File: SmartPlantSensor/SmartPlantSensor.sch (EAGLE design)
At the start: 13 parts

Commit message: Release v1.0.0
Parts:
- removed C5: 10nF, rcl:C-EUC0603
- removed U$1: TLC555CDR, HeRo:TLC555CDR
- removed U$2: ESP-12E, HeRo:ESP-12E
- added C1: 10nF, rcl:C-EUC0603
- added DS18B20: DS18B20Z+, MaximIntegrated:DS18B20Z+
- added ESP-12E: ESP-12E, ESP:ESP-12E
- added JP10, JP11, JP12, JP13, JP14, JP3, JP4, JP5, JP6, JP7, JP8, JP9: (no value), pinhead:PINHD-1X1
- added R10, R11, R7, R8, R9: 10k, rcl:R-EU_R0603
- added TLC555: TLC555CD, TexasInstruments:TLC555CD
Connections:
- removed net N$7: C5.2, U$1.CONT
- new net 1WIRE: DS18B20.DQ, ESP-12E.IO4
- new net EN: ESP-12E.EN, R7.1
- new net IO0: ESP-12E.IO0, JP6.1, R9.1
- new net IO12: ESP-12E.IO12, JP12.1
- new net IO13: ESP-12E.IO13, JP11.1
- new net IO14: ESP-12E.IO14, JP13.1
- new net IO15: ESP-12E.IO15, R8.2
- new net IO16: ESP-12E.IO16, JP14.1
- new net IO2: ESP-12E.IO2, R11.1
- new net N$1: C1.2, TLC555.CONT
- new net RST: ESP-12E.RST, JP5.1, R10.1
- new net RXD: ESP-12E.RXD, JP8.1
- new net TXD: ESP-12E.TXD, JP7.1
- net +3V3: now also DS18B20.VDD, ESP-12E.VCC, JP3.1, JP9.1, R10.2, R11.2, R7.2, R9.2, TLC555.RST, TLC555.VDD; no longer U$1.RESET, U$1.VDD, U$2.VCC
- net ADC: now also ESP-12E.ADC; no longer U$2.ADC
- net DISH: now also TLC555.DISCH; no longer U$1.DISCH
- net GND: now also C1.1, DS18B20.GND, ESP-12E.GND, JP10.1, JP4.1, R8.1, TLC555.GND; no longer C5.1, U$1.GND, U$2.GND
- net OUT: now also TLC555.OUT; no longer U$1.OUT
- net T: now also TLC555.THRES, TLC555.TRIG; no longer U$1.THRES, U$1.TRIG
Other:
- note added: "Capacitive Moisture Sensor"
- note added: "ESP8266"
- note added: "ESP8266 I/O"
- note added: "ESP8266 PU/PD"
- note added: "Smart Plant Sensor"
- note added: "Temperature-Sensor"
- note added: "Voltage divider: 3.3V -> 1V"
- note added: "https://github.com/xXAM22Xx/SmartPlantSensor"
- note added: "v1.0.0"
- moved on the sheet: C3, C4, R1, R4, R5, R6

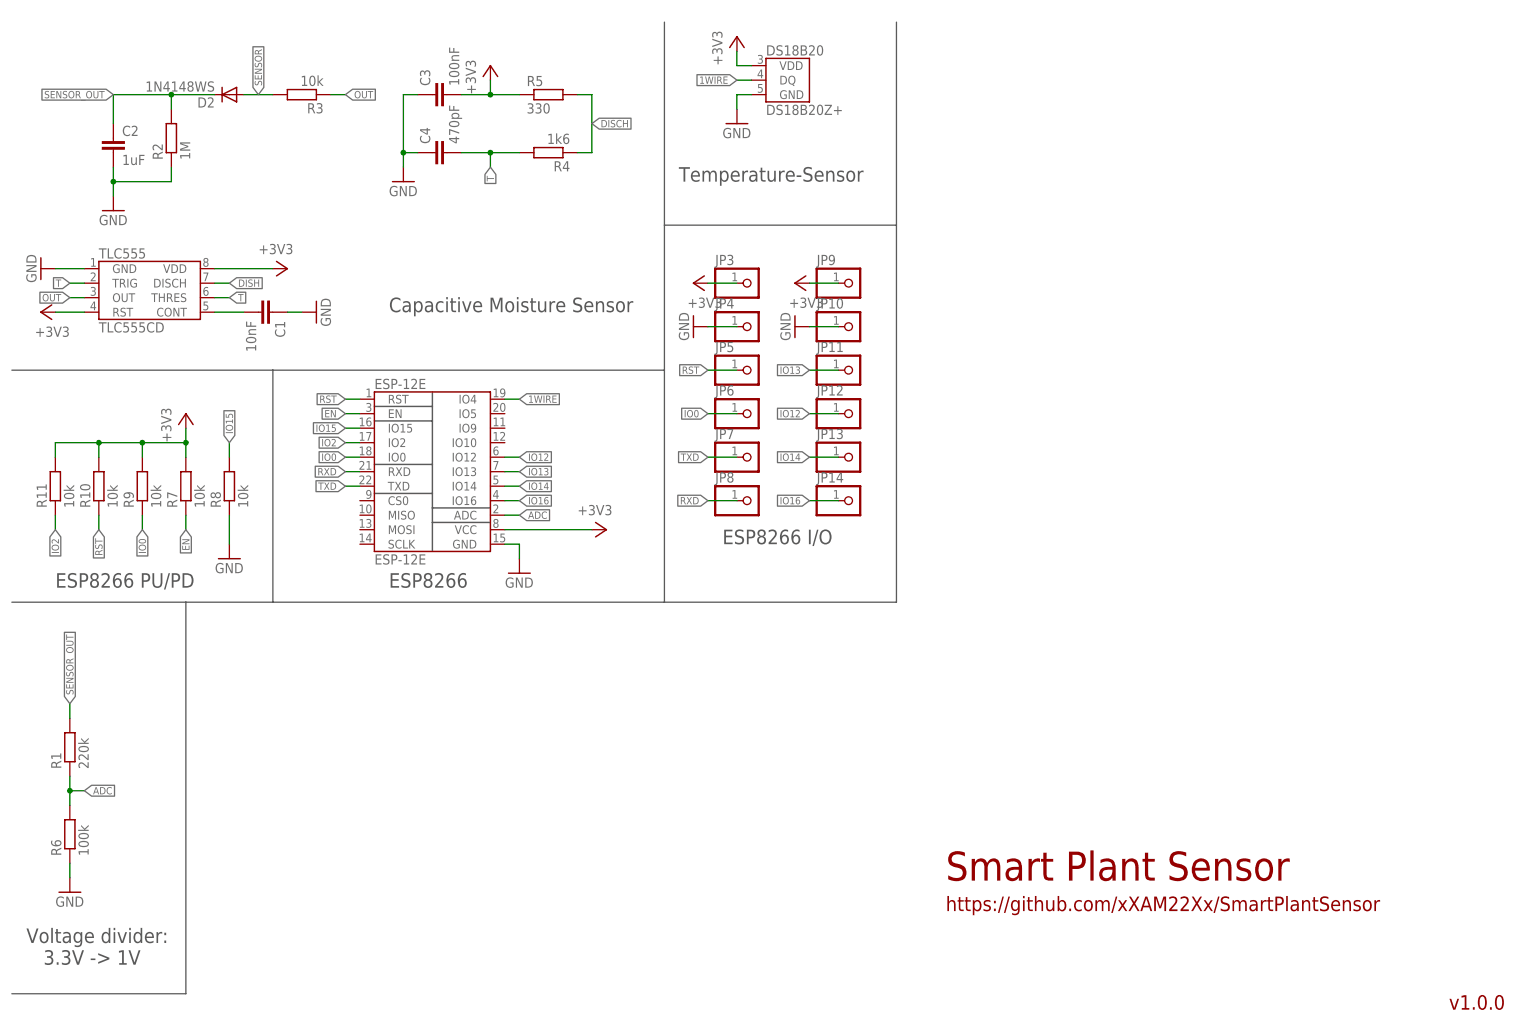
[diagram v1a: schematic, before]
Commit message: Reworked Layout, added Protection
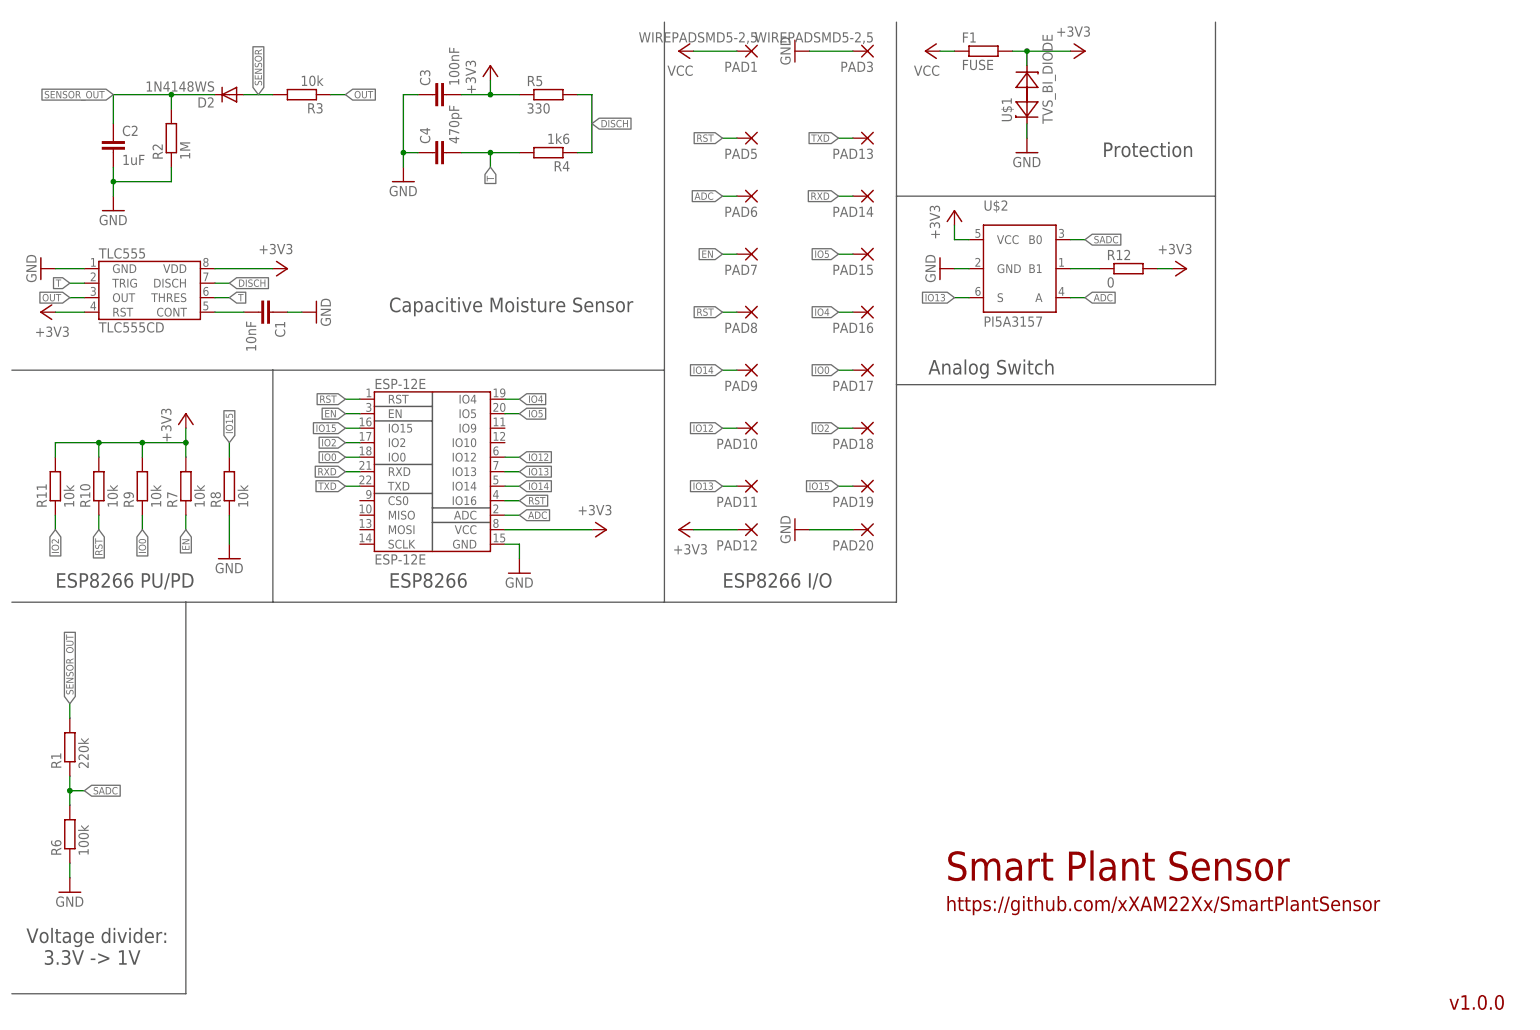
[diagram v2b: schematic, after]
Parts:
- removed DS18B20: DS18B20Z+, MaximIntegrated:DS18B20Z+
- removed JP10, JP11, JP12, JP13, JP14, JP3, JP4, JP5, JP6, JP7, JP8, JP9: (no value), pinhead:PINHD-1X1
- added F1: FUSE, rcl:R-EU_R1206
- added PAD1, PAD3: WIREPADSMD5-2,5, wirepad:WIREPADSMD5-2,5
- added PAD10, PAD11, PAD12, PAD13, PAD14, PAD15, PAD16, PAD17, PAD18, PAD19, PAD20, PAD5, PAD6, PAD7, PAD8, PAD9: (no value), wirepad:SMD2
- added R12: 0, rcl:R-EU_R0402
- added U$1: TVS_BI_DIODE, HeRo:TVS_BI_DIODE
- added U$2: PI5A3157, HeRo:PI5A3157
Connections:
- removed net 1WIRE: DS18B20.DQ, ESP-12E.IO4
- removed net DISH: TLC555.DISCH
- removed net IO16: ESP-12E.IO16, JP14.1
- new net IO4: ESP-12E.IO4, PAD16.P
- new net IO5: ESP-12E.IO5, PAD15.P
- new net N$4: R12.1, U$2.B1
- new net SADC: R1.1, R6.2, U$2.B0
- new net VCC: F1.1, PAD1.P
- net +3V3: now also F1.2, PAD12.P, R12.2, U$1.C, U$2.VCC; no longer DS18B20.VDD, JP3.1, JP9.1
- net ADC: now also PAD6.P, U$2.A; no longer R1.1, R6.2
- net DISCH: now also TLC555.DISCH
- net EN: now also PAD7.P
- net GND: now also PAD20.P, PAD3.P, U$1.A, U$2.GND; no longer DS18B20.GND, JP10.1, JP4.1
- net IO0: now also PAD17.P; no longer JP6.1
- net IO12: now also PAD10.P; no longer JP12.1
- net IO13: now also PAD11.P, U$2.S; no longer JP11.1
- net IO14: now also PAD9.P; no longer JP13.1
- net IO15: now also PAD19.P
- net IO2: now also PAD18.P
- net RST: now also ESP-12E.IO16, PAD5.P, PAD8.P; no longer JP5.1
- net RXD: now also PAD14.P; no longer JP8.1
- net TXD: now also PAD13.P; no longer JP7.1
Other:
- note added: "Analog Switch"
- note added: "Protection"
- note removed: "Temperature-Sensor"
